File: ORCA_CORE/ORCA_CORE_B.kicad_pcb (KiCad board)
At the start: 2 copper layers, 218 x 99 mm, 201 parts, among them J1 Vext_in, J10 Raspberry_Pi_2_3, J11 wheel_left, J12 md_out, J13 md_out, J14 limit_sw_upper, J15 limit_sw_upper, J16 limit_sw_under, J17 data_line_power, J18 +6V_motor, J19 +5Vin_cpu, J2 6Vout, J20 limit_sw_under, J21 Vin_motor, J22 Vin_motor, J23 md_arm, J24 md_fork, J25 servo_arm, J26 Vin_motor, J3 6Vout, J31 I2C_1, J32 I2C_2, J33 cpu_female_left, J34 cpu_female_right, J35 hat_male_right, J36 enable_arm, J37 enable_arm, J38 servo_arm, J39 md_arm, J4 6Vout, J40 md_fork, J41 cpu_male_left, J42 uart, J43 uart_device, J44 servo_camera, J45 reset, J46 reset, J47 led, J48 led, J49 USB_B_Micro, J5 6Vin, J50 USB_A, J51 usb_A_device, J52 usb_A, J53 cover_left, J54 base_left, J55 servo connectors, J59 base_right, J6 Vext_out, J60 cover_right, J7 6Vout, J8 wheel_front, J9 wheel_right, P1 USB_C_Receptacle_USB2.0, Q1 BSS138, Q2 BSS138, Q3 TJ60S04M3L, Q8 BSS138, SW2 REST_sw, U1 FT230XS, U10 TLP293, U11 TLP293, U12 TLP293, U13 TLP293, U14 BNO055, U15 TLP293, U16 TLP293, U17 AZ1117-3.3, U18 TLP293, U19 TLP293, U2 PCA9685PW_Q900_118, U20 TLP293, U21 TLP293, U22 AZ1117-3.3, U23 TLP293, U24 TLP293, U25 TLP293, U26 PMW3360, U3 AM2837, U4 AM2837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

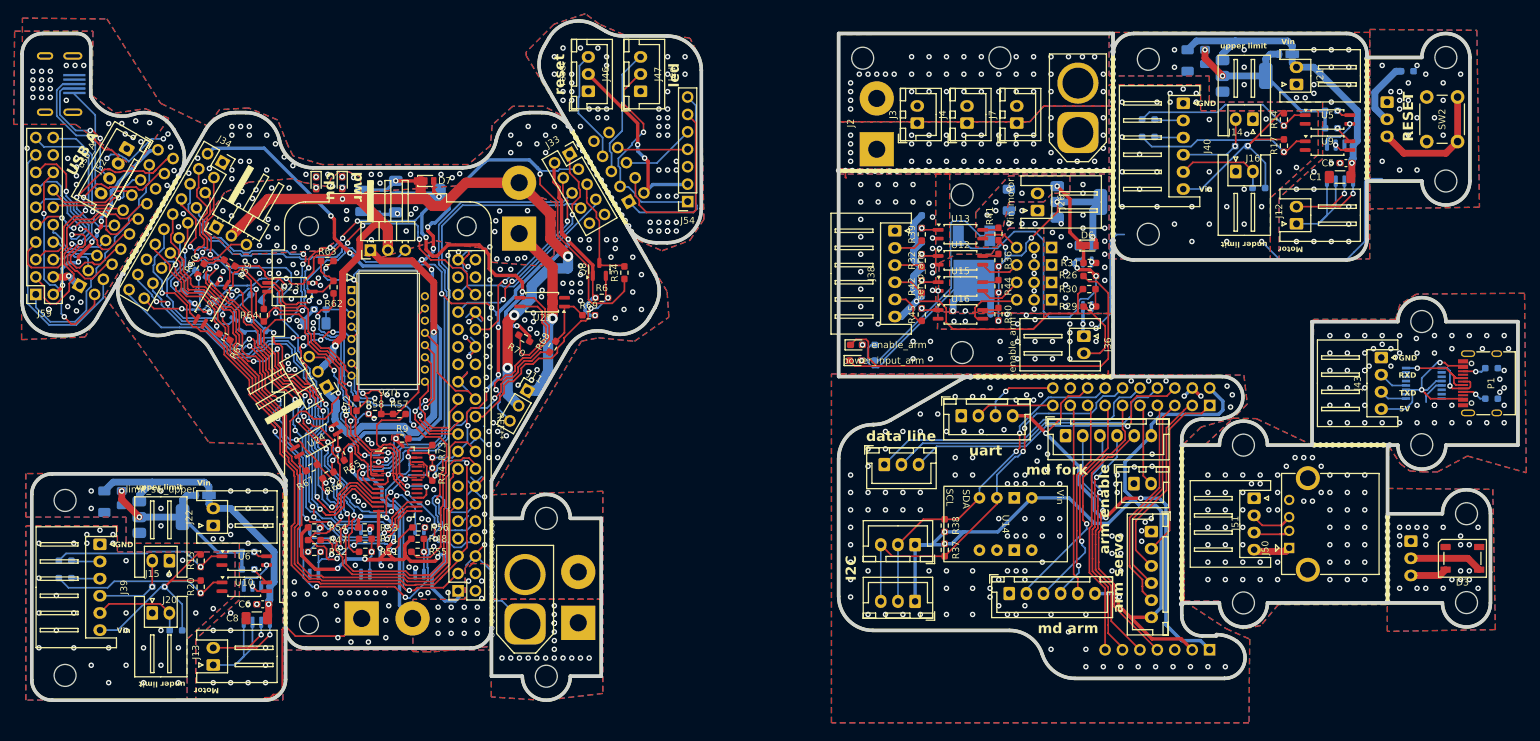
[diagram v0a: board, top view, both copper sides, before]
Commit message: correct few errors in usp
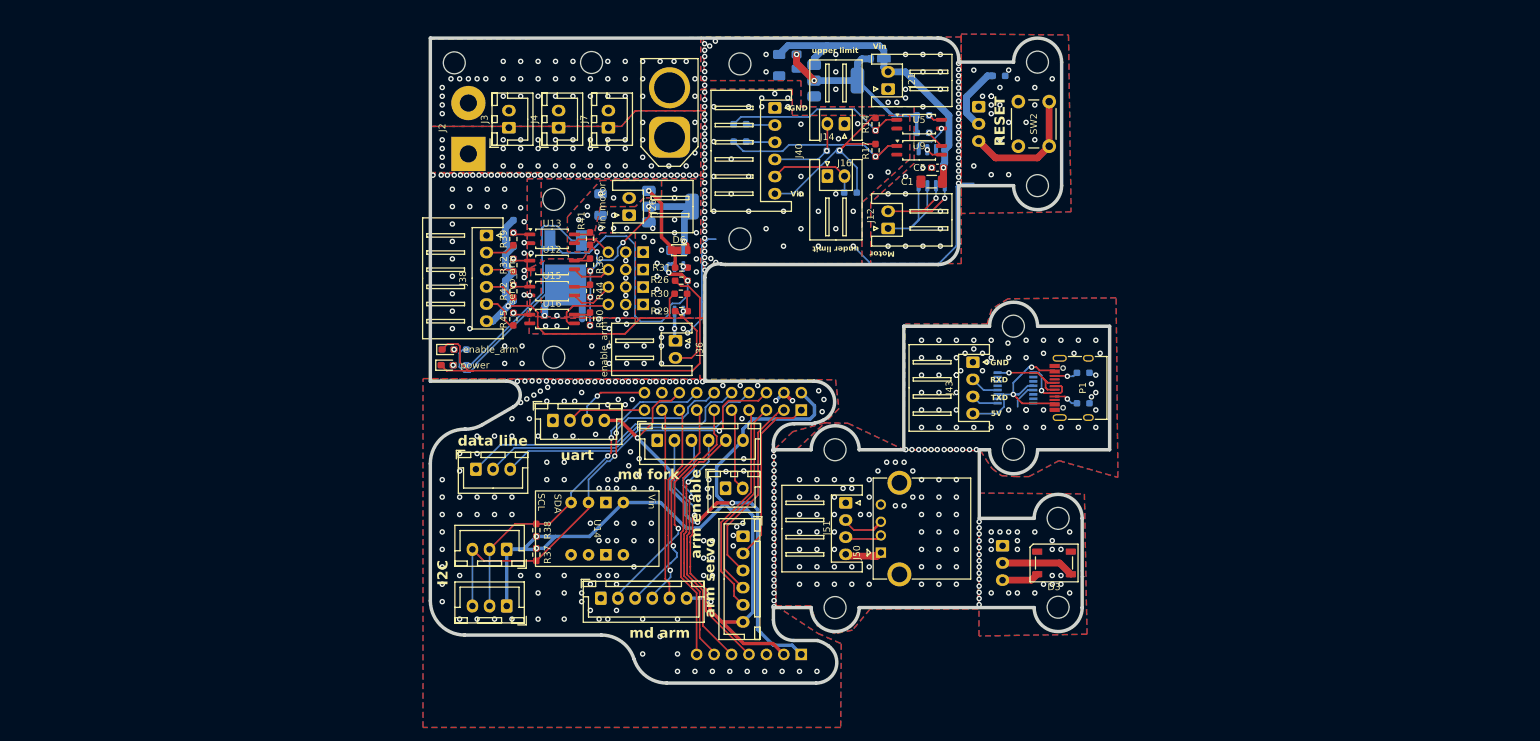
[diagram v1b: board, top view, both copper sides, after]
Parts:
- removed C11, C3: 10u/50V, Capacitor_SMD:C_1206_3216Metric_Pad1.33x1.80mm_HandSolder
- removed C12, C4: 22u25V, Capacitor_SMD:C_0805_2012Metric_Pad1.18x1.45mm_HandSolder
- removed C13, C6: 0.1u, Capacitor_SMD:C_0603_1608Metric_Pad1.08x0.95mm_HandSolder
- removed C14: 10u, Capacitor_SMD:C_1206_3216Metric_Pad1.33x1.80mm_HandSolder
- removed C8: 220u, Capacitor_SMD:C_1206_3216Metric_Pad1.33x1.80mm_HandSolder
- removed D19: pwr_cpu, LED_SMD:LED_0603_1608Metric_Pad1.05x0.95mm_HandSolder
- removed D2, D7: CUHS20560, Diode:Diode_US2H
- removed D8: pwr_motor, LED_SMD:LED_0603_1608Metric_Pad1.05x0.95mm_HandSolder
- removed G***: LOGO, Logo:ORCA_logo_large
- removed H15, H16: Hole_md, MountingHole:MountingHole_3.2mm_M3
- removed H7, H8: Hole_Vext, MountingHole:MountingHole_3.2mm_M3
- removed J1: Vext_in, Conn:AMASS_XT60_Vertifcal_withmodel_female
- removed J10: Raspberry_Pi_2_3, cpu:raspberrypi_Zerp_W_horisontal
- removed J11: wheel_left, Connector_PinHeader_2.54mm:PinHeader_1x03_P2.54mm_Vertical
- removed J13: md_out, Connector_JST:JST_XH_S2B-XH-A_1x02_P2.50mm_Horizontal
- removed J15: limit_sw_upper, Connector_JST:JST_XH_S2B-XH-A_1x02_P2.50mm_Horizontal
- removed J18: +6V_motor, Conn:power_pad
- removed J19: +5Vin_cpu, Conn:power_pad
- removed J20: limit_sw_under, Connector_JST:JST_XH_S2B-XH-A_1x02_P2.50mm_Horizontal
- removed J22: Vin_motor, Connector_JST:JST_XH_S2B-XH-A_1x02_P2.50mm_Horizontal
- removed J33: cpu_female_left, Connector_PinSocket_2.54mm:PinSocket_2x05_P2.54mm_Vertical
- removed J34: cpu_female_right, Connector_PinSocket_2.54mm:PinSocket_2x10_P2.54mm_Vertical
- removed J35: hat_male_right, Connector_PinHeader_2.54mm:PinHeader_2x10_P2.54mm_Vertical
- removed J39: md_arm, Connector_JST:JST_XH_S6B-XH-A_1x06_P2.50mm_Horizontal
- removed J41: cpu_male_left, Connector_PinHeader_2.54mm:PinHeader_2x05_P2.54mm_Vertical
- removed J44: servo_camera, Connector_PinHeader_2.54mm:PinHeader_1x03_P2.54mm_Horizontal
- removed J46: reset, Connector_JST:JST_XH_B3B-XH-A_1x03_P2.50mm_Vertical
- removed J47: led, Connector_JST:JST_XH_B3B-XH-A_1x03_P2.50mm_Vertical
- removed J49: USB_B_Micro, Conn:ZX60-B-5S(31)
- removed J52: usb_A, Connector_JST:JST_XH_B4B-XH-A_1x04_P2.50mm_Vertical
- removed J54: base_left, Connector_PinSocket_2.54mm:PinSocket_1x07_P2.54mm_Vertical
- removed J59: base_right, Connector_PinSocket_2.54mm:PinSocket_2x10_P2.54mm_Vertical
- removed J6: Vext_out, Conn:power_pad
- removed J8: wheel_front, Connector_PinHeader_2.54mm:PinHeader_1x03_P2.54mm_Horizontal
- removed J9: wheel_right, Connector_PinHeader_2.54mm:PinHeader_1x03_P2.54mm_Horizontal
- removed Q1, Q2, Q8: BSS138, Package_TO_SOT_SMD:SOT-23
- removed R11, R19, R51, R52, R55, R59, R62, R65, R68: 100, Resistor_SMD:R_0603_1608Metric_Pad0.98x0.95mm_HandSolder
- removed R13, R15, R20, R21, R23, R25, R34, R4, R47, R48, R5, R53, R54, R56, R6, R60, R61, R63, R64, R66, R67, R69, R7, R70, R71, R73, R74, R8: 2.2k, Resistor_SMD:R_0603_1608Metric_Pad0.98x0.95mm_HandSolder
- removed R35, R49: 1k, Resistor_SMD:R_0603_1608Metric_Pad0.98x0.95mm_HandSolder
- removed R57: 1.2k, Resistor_SMD:R_0603_1608Metric_Pad0.98x0.95mm_HandSolder
- removed R58: 2k, Resistor_SMD:R_0603_1608Metric_Pad0.98x0.95mm_HandSolder
- removed R72, R9: 10k, Resistor_SMD:R_0603_1608Metric_Pad0.98x0.95mm_HandSolder
- removed U10, U18, U19, U20, U21, U23, U24, U25, U6: TLP293, Package_SO:SOIC-4_4.55x2.6mm_P1.27mm
- removed U2: PCA9685PW_Q900_118, digikey-footprints:TSSOP-28_W4.40mm
- removed U22, U8: AZ1117-3.3, Package_TO_SOT_SMD:SOT-223-3_TabPin2
- removed U26: PMW3360, mouse_sensor:PMW3360
- removed U4: AM2837, Package_SO:SOP-8_3.9x4.9mm_P1.27mm
- D5: value power_input_arm -> power
- moved C1 59.5 mm to (170.6, 63.9)
- moved C10 59.5 mm to (133.5, 73.9)
- moved C2 59.5 mm to (150.9, 46.4)
- moved C7 59.5 mm to (148.3, 46.9)
- moved D1 59.5 mm to (162.9, 46.0)
- moved D3 59.5 mm to (188.4, 119.5)
- moved D4 59.5 mm to (100.1, 88.4)
- moved D5 59.5 mm to (99.9, 90.7)
- moved D6 59.5 mm to (133.8, 73.9)
- moved H1 59.5 mm to (182.5, 85.0)
- moved H13 59.5 mm to (142.6, 72.3)
- moved H14 59.5 mm to (142.6, 46.8)
- moved H2 59.5 mm to (182.5, 102.9)
- moved H23 59.5 mm to (156.5, 103.0)
- moved H24 59.5 mm to (156.5, 126.0)
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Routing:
- net +3V3: track 398.8 -> 70.5 mm, vias 43 -> 9
- net +5V: track 206.0 -> 0.00 mm, vias 25 -> 0
- net +6V: track 227.1 -> 44.6 mm, vias 8 -> 1
- net +3V3_motor: track 167.6 -> 0.00 mm, vias 18 -> 0
- net GND1: track 208.7 -> 57.3 mm, vias 738 -> 552
- net SDA: track 113.6 -> 0.00 mm, vias 3 -> 0
- net SCL: track 111.7 -> 0.00 mm, vias 2 -> 0
- net /cpu/GPIO18: track 104.6 -> 0.00 mm, vias 4 -> 0
- net /cpu/GPIO17: track 102.4 -> 0.00 mm, vias 2 -> 0
- net GND: track 146.7 -> 61.2 mm, vias 113 -> 49
- net /cpu/emerge_detector: track 80.3 -> 0.00 mm, vias 9 -> 0
- net RXD_3V3: track 79.0 -> 0.00 mm, vias 6 -> 0
- net /cpu/emerge_order: track 76.6 -> 0.00 mm, vias 7 -> 0
- net /cpu/LED6: track 76.0 -> 0.00 mm, vias 2 -> 0
- net /cpu/LED8: track 75.6 -> 0.00 mm, vias 3 -> 0
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- removed copper zone on B.Cu, net +5V
- removed copper zone on F.Cu, net +5V
- removed copper zone on B.Cu, net /cpu_hat/GND_usb
- removed copper zone on F.Cu, net /cpu_hat/GND_usb
- removed copper zone on B.Cu, net Net-(J1-Pin_2)
- removed copper zone on F.Cu, net Net-(J1-Pin_2)
- removed copper zone on F.Cu, net Net-(U2-A0)
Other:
- board size 218 x 99 mm -> 99 x 94 mm
- board text removed: "ORCA_CORE core_board v0 2025/04/21"
- board text removed: "USB A"
- board text removed: "cpu"
- board text removed: "led"
- board text removed: "limit_sw_under"
- board text removed: "pwr"
- board text removed: "reset"
